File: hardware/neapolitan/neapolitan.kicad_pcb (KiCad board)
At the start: 4 copper layers, 120 x 75 mm, 253 parts, among them J1 USB-MICRO-B, J10 GND_CLIP, J11 BARREL_JACK, J2 RF-SHIELD-FRAME, J3 RF-SHIELD-COVER, J4 MOUNTING_HOLE, J5 MOUNTING_HOLE, J6 MOUNTING_HOLE, J7 MOUNTING_HOLE, J8 MOUNTING_HOLE, J9 MOUNTING_HOLE, P1 !IO_INT, P13 GPO1, P14 XCVR_CLKOUT, P15 INTR, P17 GPO6, P18 OEB, P19 GPO3, P2 !IO_RESET, P20 GPIO, P21 REF_IN, P22 I2S, P27 MIXER_SDATA, P28 SD, P31 MIXER_SCLK, P32 MIXER_ENX, P33 MIXER_RESETX, P34 MIX_BYPASS, P35 !MIX_BYPASS, P36 VAA, P37 SCL, P38 SDA, P39 SSP0_SCK, P4 ANTENNA, P40 SSP0_MOSI, P41 SSP0_MISO, P42 TX, P43 RX, P44 HP, P45 LP, P46 TX_MIX_BP, P47 RX_MIX_BP, P48 TX_AMP, P49 RX_AMP, P5 LEDS, P50 AMP_BYPASS, P51 !TX_AMP_PWR, P52 !RX_AMP_PWR, P53 CS_XCVR, P55 TXENABLE, P56 RXENABLE, P57 XTAL2, P6 GPO4, P67 RSSI, P7 GPO2, P80 SHIELD, P83 GND, P84 GND, P85 GND, P86 GND, P87 GND, P88 GND, P89 GND, P9 BASEBAND, P90 GND, P91 GND, P92 GND, Q1 MOSFET_P, Q2 MOSFET_P, Q3 MOSFET_P, Q4 MOSFET_P, T1 MIX_IN_BALUN, T2 MIX_OUT_BALUN, T3 RX_BALUN, T4 TX_BALUN, U1 SKY13350, U10 SKY13350, U11 SKY13350, U12 SKY13317, U13 MGA-81563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

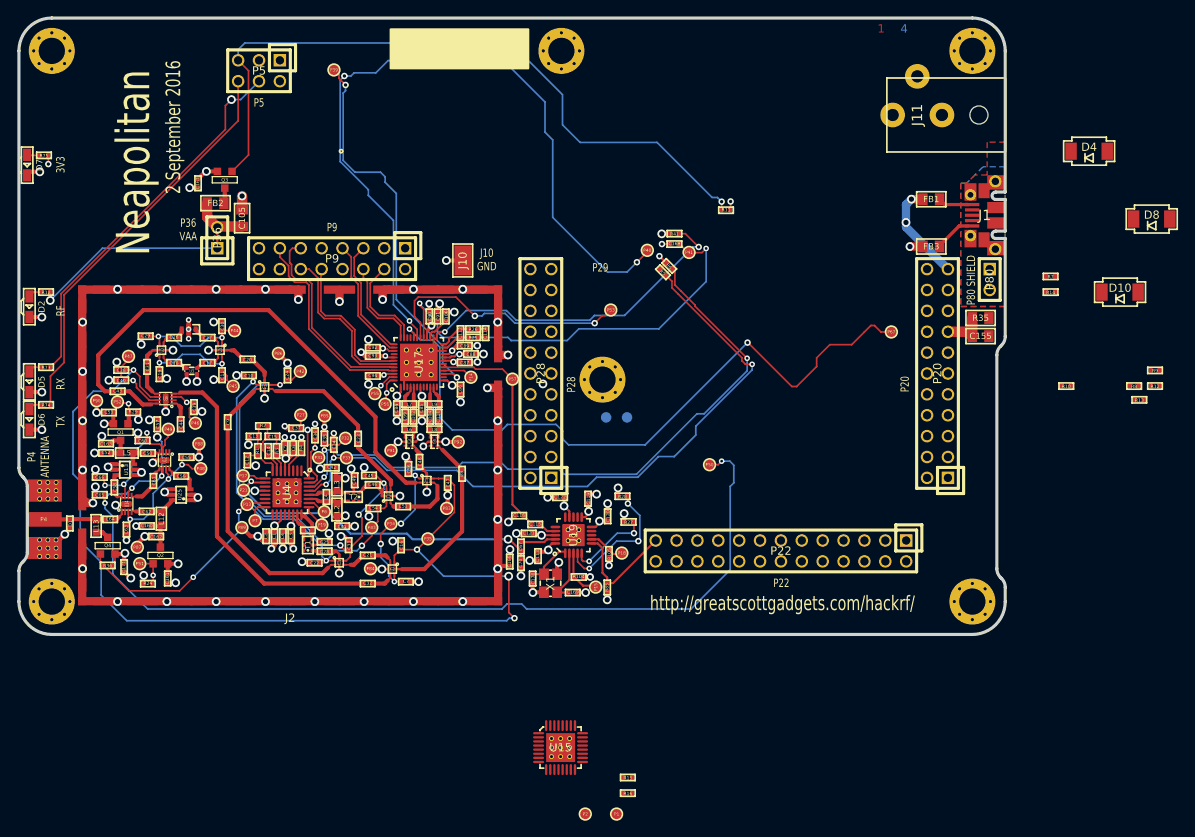
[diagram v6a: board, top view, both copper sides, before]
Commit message: Neapolitan: completed initial layout
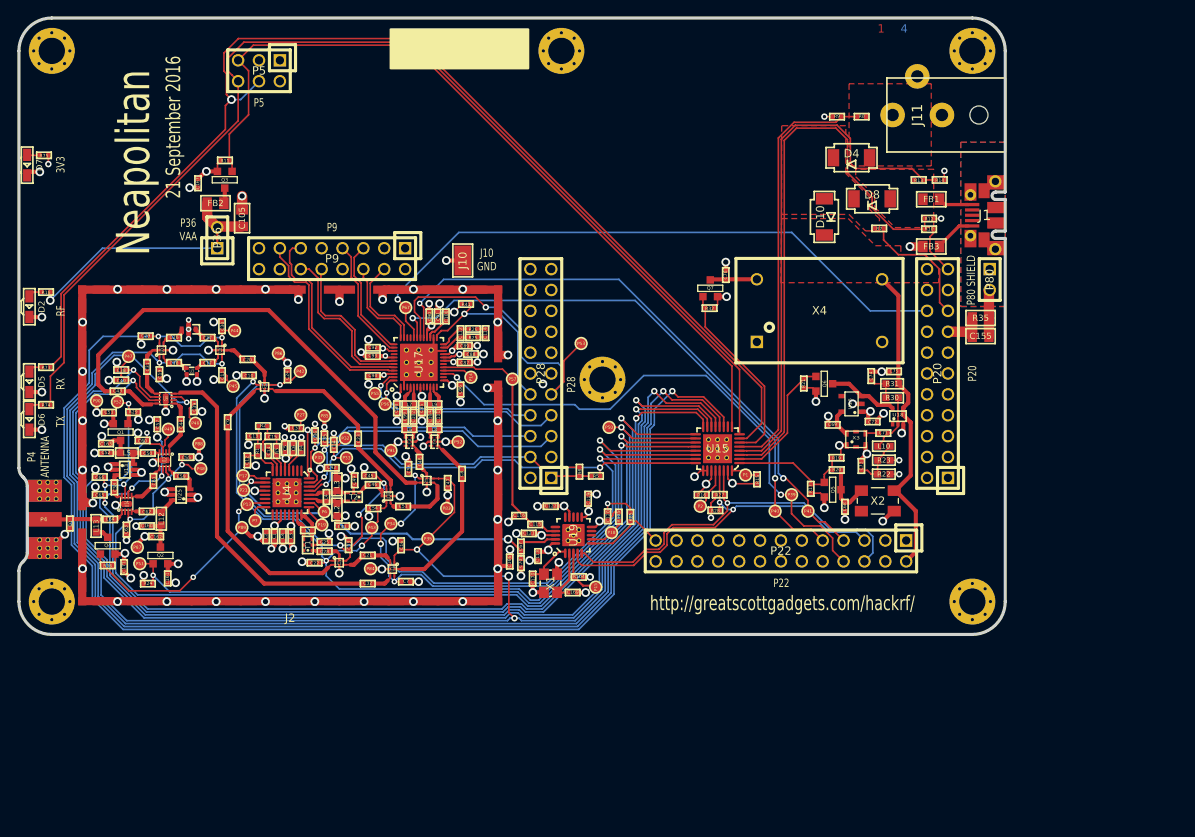
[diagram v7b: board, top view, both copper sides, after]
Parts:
- removed C168: 100pF, hackrf:GSG-0402
- removed P37: SCL, hackrf:GSG-TESTPOINT-50MIL
- removed P38: SDA, hackrf:GSG-TESTPOINT-50MIL
- added C68: 100nF, hackrf:GSG-0402, F.Cu at (160.5, 159.5)
- added C69: 1uF, hackrf:GSG-0402, F.Cu at (159.0, 149.5)
- added C71: 10nF, hackrf:GSG-0402, F.Cu at (165.2, 150.5)
- added C72: 100nF, hackrf:GSG-0402, F.Cu at (163.9, 149.1)
- added C73: 10nF, hackrf:GSG-0402, F.Cu at (162.5, 154.5)
- added C74: 10nF, hackrf:GSG-0402, F.Cu at (163.7, 143.6)
- added C75: 22pF, hackrf:GSG-0402, F.Cu at (166.5, 143.0)
- added C76: 10nF, hackrf:GSG-0402, F.Cu at (146.0, 131.3)
- added L10: 10uH, hackrf:GSG-0603, F.Cu at (165.2, 152.1)
- added Q5: MOSFET_P, gsg-modules:SOT23GDS, F.Cu at (159.0, 157.4)
- added Q6: MOSFET_P, gsg-modules:SOT23GDS, F.Cu at (158.0, 144.5)
- added Q7: MOSFET_P, gsg-modules:SOT23GDS, F.Cu at (144.1, 132.9)
- added R17: 10k, hackrf:GSG-0402, F.Cu at (156.3, 157.3)
- added R19: 10k, hackrf:GSG-0402, F.Cu at (159.5, 153.5)
- added R20: 0, hackrf:GSG-0402, F.Cu at (159.5, 155.0)
- added R21: 10k, hackrf:GSG-0402, F.Cu at (155.5, 144.5)
- added R22: 470k, hackrf:GSG-0603, F.Cu at (165.2, 155.5)
- added R23: 470k, hackrf:GSG-0603, F.Cu at (165.2, 153.8)
- added R30: 470k, hackrf:GSG-0603, F.Cu at (166.2, 146.2)
- added R31: 470k, hackrf:GSG-0603, F.Cu at (166.2, 144.5)
- added R32: 10k, hackrf:GSG-0402, F.Cu at (144.0, 135.3)
- added U16: TCR2EF, gsg-modules:SOT25, F.Cu at (161.3, 146.9)
- added U18: 74LVC1G14, gsg-modules:SOT353-1, F.Cu at (166.9, 148.4)
- added X2: FOX924B, gsg-modules:XTAL5.0x3.2mm, F.Cu at (164.5, 158.8)
- added X3: KT2520, gsg-modules:KT2520K, F.Cu at (161.8, 151.3)
- added X4: OH4, gsg-modules:OH4, F.Cu at (157.4, 135.6)
- moved P39 76.0 mm to (154.0, 158.0)
- moved R11 61.3 mm to (85.1, 117.3), turned to 0 degrees
- moved P67 59.2 mm to (107.1, 135.2)
- moved R9 49.5 mm to (159.5, 112.0), turned to 180 degrees
- moved R8 46.6 mm to (162.5, 112.0), turned to 180 degrees
- moved P1 44.1 mm to (148.4, 155.6)
- moved U15 41.1 mm to (145.0, 152.4), turned to 180 degrees
- moved P2 40.0 mm to (142.9, 159.4)
- moved R15 39.5 mm to (149.8, 156.1), turned to 90 degrees
- moved R13 37.9 mm to (169.5, 119.7)
- moved R16 37.4 mm to (143.1, 158.0)
- moved D10 37.1 mm to (158.0, 124.2), turned to 90 degrees
- moved P40 35.3 mm to (152.0, 160.0)
- moved P41 34.6 mm to (156.0, 160.0)
- moved R12 34.2 mm to (170.7, 124.4)
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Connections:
- net Net-(D10-Pad2) renamed /mcu/usb/power/DIODE_TOWN
- P22 pad 2: (no net) -> CLKIN
- P28 pad 7: RXENABLE -> TXENABLE
- P28 pad 8: TXENABLE -> RXENABLE
- U15 pad 1: HP -> /mcu/usb/power/X2_ENABLE
- U15 pad 10: TX_AMP -> (no net)
- U15 pad 11: !RX_AMP_PWR -> HP
- U15 pad 12: !TX_AMP_PWR -> LP
- U15 pad 13: AMP_BYPASS -> TX_MIX_BP
- U15 pad 14: MIXER_RESETX -> !MIX_BYPASS
- U15 pad 15: !VAA_ENABLE -> RX_MIX_BP
- U15 pad 16: (no net) -> !RX_AMP_PWR
- U15 pad 17: /mcu/usb/power/LED2 -> RX_AMP
- U15 pad 18: /mcu/usb/power/LED3 -> AMP_BYPASS
- U15 pad 19: (no net) -> TX_AMP
- U15 pad 2: LP -> /mcu/usb/power/X3_ENABLE
- U15 pad 20: (no net) -> !TX_AMP_PWR
- U15 pad 21: (no net) -> RX
- U15 pad 22: /mcu/usb/power/VBUS_SENSE -> MIX_BYPASS
- U15 pad 23: /mcu/usb/power/VBUS2_SENSE -> TX
- U15 pad 24: /mcu/usb/power/BARREL_SENSE -> MIXER_RESETX
- U15 pad 3: RX -> /mcu/usb/power/VBUS_SENSE
- U15 pad 4: TX -> /mcu/usb/power/VBUS2_SENSE
- U15 pad 5: MIX_BYPASS -> /mcu/usb/power/BARREL_SENSE
- U15 pad 6: !MIX_BYPASS -> /mcu/usb/power/X4_ENABLE
- U15 pad 7: RX_MIX_BP -> /mcu/usb/power/LED2
- U15 pad 8: TX_MIX_BP -> /mcu/usb/power/LED3
- U15 pad 9: RX_AMP -> !VAA_ENABLE
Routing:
- net TX_MIX_BP: track 5.87 -> 151.7 mm, vias 1 -> 2
- net HP: track 14.2 -> 159.3 mm, vias 2 -> 3
- net LP: track 14.8 -> 156.9 mm, vias 2 -> 3
- net RX_MIX_BP: track 8.74 -> 137.7 mm, vias 1 -> 2
- net !RX_AMP_PWR: track 3.94 -> 126.0 mm, vias 1 -> 2
- net RX_AMP: track 18.8 -> 124.1 mm, vias 3 -> 4
- net /mcu/usb/power/LED2: track 46.0 -> 143.6 mm
- net TX_AMP: track 17.2 -> 112.5 mm, vias 3 -> 4
- net /mcu/usb/power/LED3: track 48.8 -> 139.7 mm
- net !TX_AMP_PWR: track 4.08 -> 84.9 mm, vias 1 -> 2
- net /mcu/usb/power/VBUS_SENSE: track 0.00 -> 69.3 mm
- net /mcu/usb/power/VBUS2_SENSE: track 0.00 -> 65.6 mm
- net RX: track 45.1 -> 110.6 mm, vias 3 -> 4
- net TX: track 51.8 -> 111.6 mm, vias 4 -> 5
- net MIX_BYPASS: track 19.8 -> 72.1 mm, vias 4 -> 5
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- added copper zone on F.Cu, net /mcu/usb/power/BARREL
- added copper zone on F.Cu, net /mcu/usb/power/DIODE_TOWN
- added copper zone on F.Cu, net /mcu/usb/power/VBUS2
- added copper zone on F.Cu, net /mcu/usb/power/VIN
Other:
- outline, holes or cut-outs redrawn
- board text added: "21 September 2016"
- board text removed: "2 September 2016"
- board text removed: "P29"

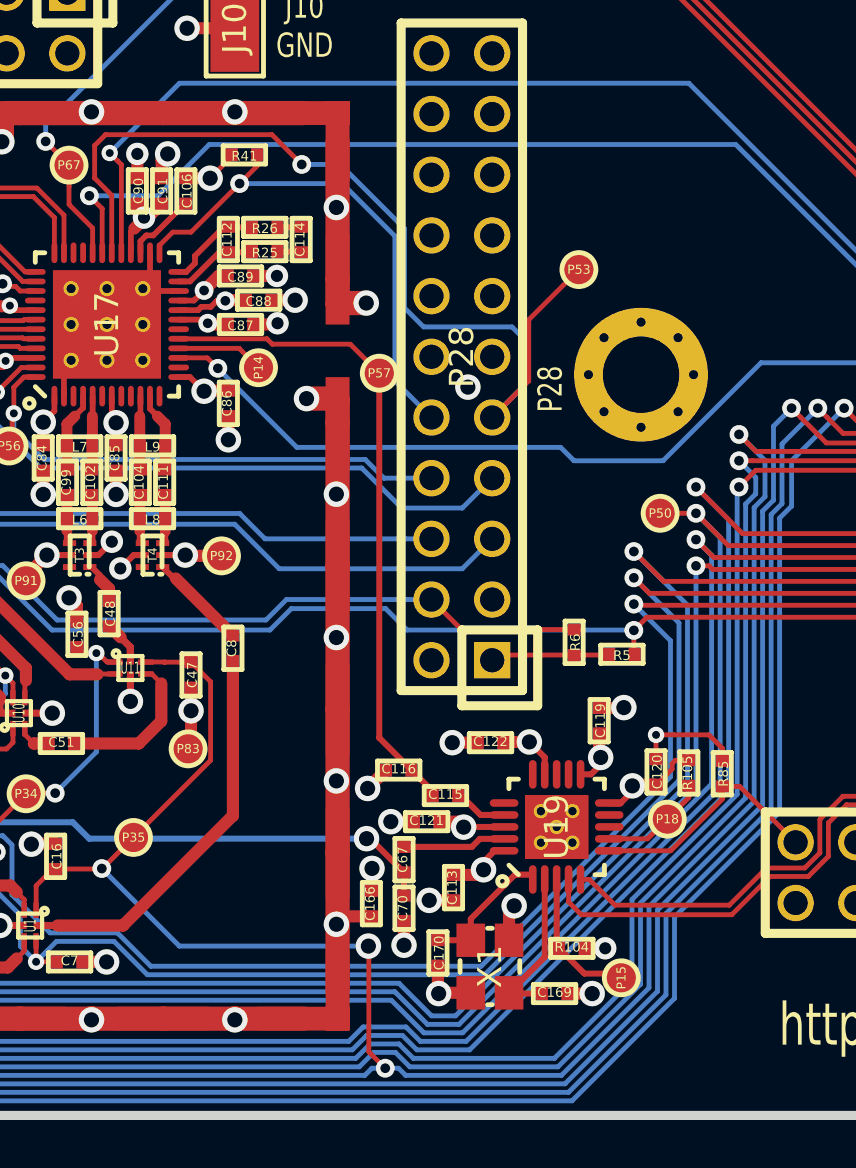
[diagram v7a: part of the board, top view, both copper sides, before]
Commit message: Neapolitan: added RF chokes to some supply pins as a noise reduction experiment
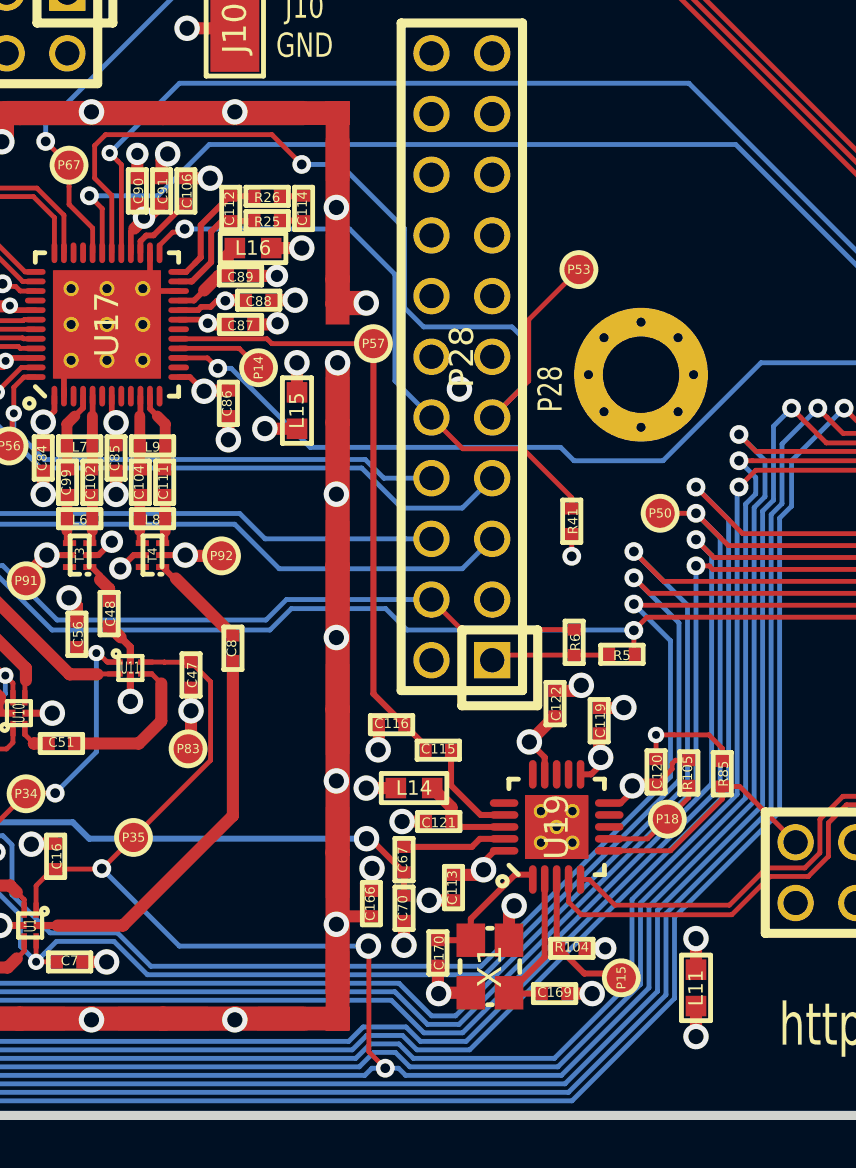
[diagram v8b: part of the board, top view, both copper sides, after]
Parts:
- added L11: 10uH, hackrf:GSG-0603, F.Cu at (133.3, 169.7)
- added L14: 10uH, hackrf:GSG-0603, F.Cu at (121.5, 161.3)
- added L15: 10uH, hackrf:GSG-0603, F.Cu at (116.6, 145.5)
- added L16: 10uH, hackrf:GSG-0603, F.Cu at (114.8, 138.7)
- moved R41 20.6 mm to (128.1, 150.1), turned to 90 degrees
- moved C122 3.16 mm to (127.4, 157.8), turned to 90 degrees
- moved C115 1.92 mm to (122.5, 159.7)
- moved C116 1.92 mm to (120.6, 158.6)
- moved C112 1.30 mm to (113.8, 137.0)
- moved R26 1.30 mm to (115.4, 136.5)
- moved C114 1.30 mm to (116.9, 137.0)
- moved R25 1.30 mm to (115.4, 137.5)
- moved P57 1.26 mm to (119.8, 142.7)
- moved C121 0.51 mm to (122.5, 162.7), turned to 0 degrees
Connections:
- C1 pad 1: VCC -> Net-(C1-Pad1)
- C121 pad 1: VCC -> GND
- C121 pad 2: GND -> Net-(C121-Pad2)
- C2 pad 1: VCC -> Net-(C1-Pad1)
- C88 pad 1: VCC -> Net-(C88-Pad1)
- C89 pad 1: VAA -> Net-(C89-Pad1)
- U17 pad 20: VCC -> Net-(C88-Pad1)
- U17 pad 21: VAA -> Net-(C89-Pad1)
- U19 pad 18: VCC -> Net-(C121-Pad2)
- U4 pad 19: VCC -> Net-(C1-Pad1)
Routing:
- net Net-(C1-Pad1): track 0.00 -> 62.6 mm, vias 0 -> 2
- net VCC: track 123.7 -> 67.9 mm
- net Net-(C88-Pad1): track 0.00 -> 8.82 mm, vias 0 -> 2
- net Net-(C121-Pad2): track 0.00 -> 4.03 mm
- net Net-(C89-Pad1): track 0.00 -> 3.77 mm
- net XCVR_EN: track 21.9 -> 25.6 mm
- net /baseband/CLK5: track 2.26 -> 4.21 mm
- net /baseband/XTAL2: track 27.6 -> 26.2 mm
- net /baseband/CPOUT+: track 3.59 -> 4.97 mm
- net /baseband/CPOUT-: track 4.04 -> 5.29 mm
- net VAA: track 68.6 -> 67.3 mm
- net GND: vias 147 -> 148
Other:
- rule trace_min: 0.1524 -> 0.006
- rule via_min_size: 0.6858 -> 0.027
